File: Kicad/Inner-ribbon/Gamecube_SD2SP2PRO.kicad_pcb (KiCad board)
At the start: 2 copper layers, 36.5 x 19 mm, 2 parts, among them J1 Conn_02x04_Odd_Even, J2 Conn_02x04_Odd_Even

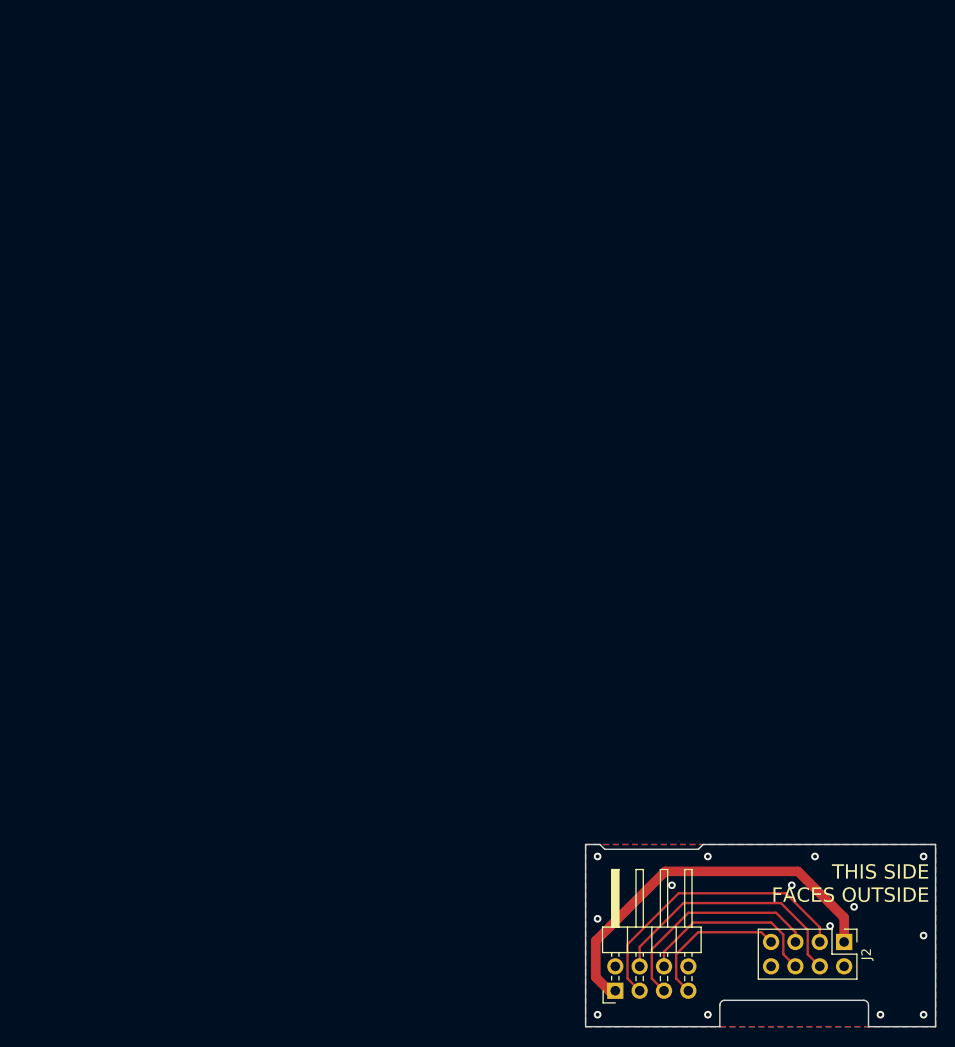
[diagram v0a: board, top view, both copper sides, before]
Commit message: fix SD2SP2 connector pinout
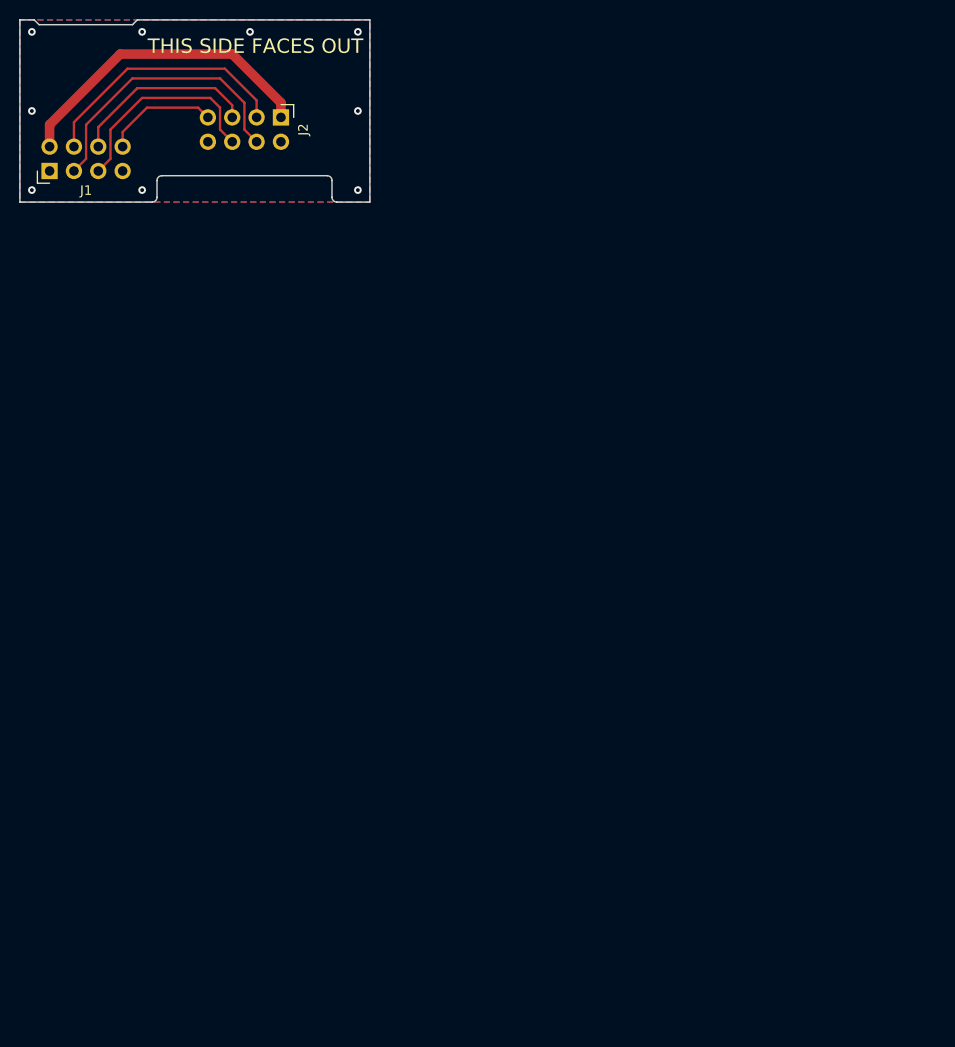
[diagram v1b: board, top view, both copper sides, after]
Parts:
- moved J2 104.1 mm to (42.3, 25.2)
- moved J1 103.9 mm to (18.2, 30.8)
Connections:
- J1 pad 1: /+3V3 -> /GND
- J1 pad 2: /GND -> /+3V3
- J1 pad 3: /INT -> /CLK
- J1 pad 4: /CLK -> /INT
- J1 pad 5: /DO -> /DI
- J1 pad 6: /DI -> /DO
- J1 pad 7: /CS -> /GND
- J1 pad 8: /GND -> /CS
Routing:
- net /+3V3: track 39.9 -> 33.1 mm
- net /CS: track 15.6 -> 11.9 mm
- net /INT: track 30.6 -> 27.1 mm
- net /DO: track 23.3 -> 19.7 mm
- net /DI: track 19.6 -> 22.1 mm
- net /CLK: track 26.9 -> 29.5 mm
- net /GND: vias 14 -> 9
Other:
- outline, holes or cut-outs redrawn
- board text added: "THIS SIDE FACES IN"
- board text added: "THIS SIDE FACES OUT"
- board text removed: "THIS SIDE FACES INSIDE"
- board text removed: "THIS SIDE FACES OUTSIDE"
